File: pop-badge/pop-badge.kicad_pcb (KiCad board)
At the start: 2 copper layers, 129.5 x 101.3 mm, 158 parts, among them J1 Conn_01x04, Q1 BC818, U1 WS2812-2020, U10 WS2812-2020, U11 WS2812-2020, U12 WS2812-2020, U13 WS2812-2020, U14 WS2812-2020, U15 WS2812-2020, U16 WS2812-2020, U17 WS2812-2020, U18 WS2812-2020, U19 WS2812-2020, U2 WS2812-2020, U20 WS2812-2020, U21 WS2812-2020, U22 WS2812-2020, U23 WS2812-2020, U24 WS2812-2020, U25 WS2812-2020, U26 Pico, U3 WS2812-2020, U4 WS2812-2020, U5 WS2812-2020, U6 WS2812-2020, U7 WS2812-2020, U8 WS2812-2020, U9 WS2812-2020

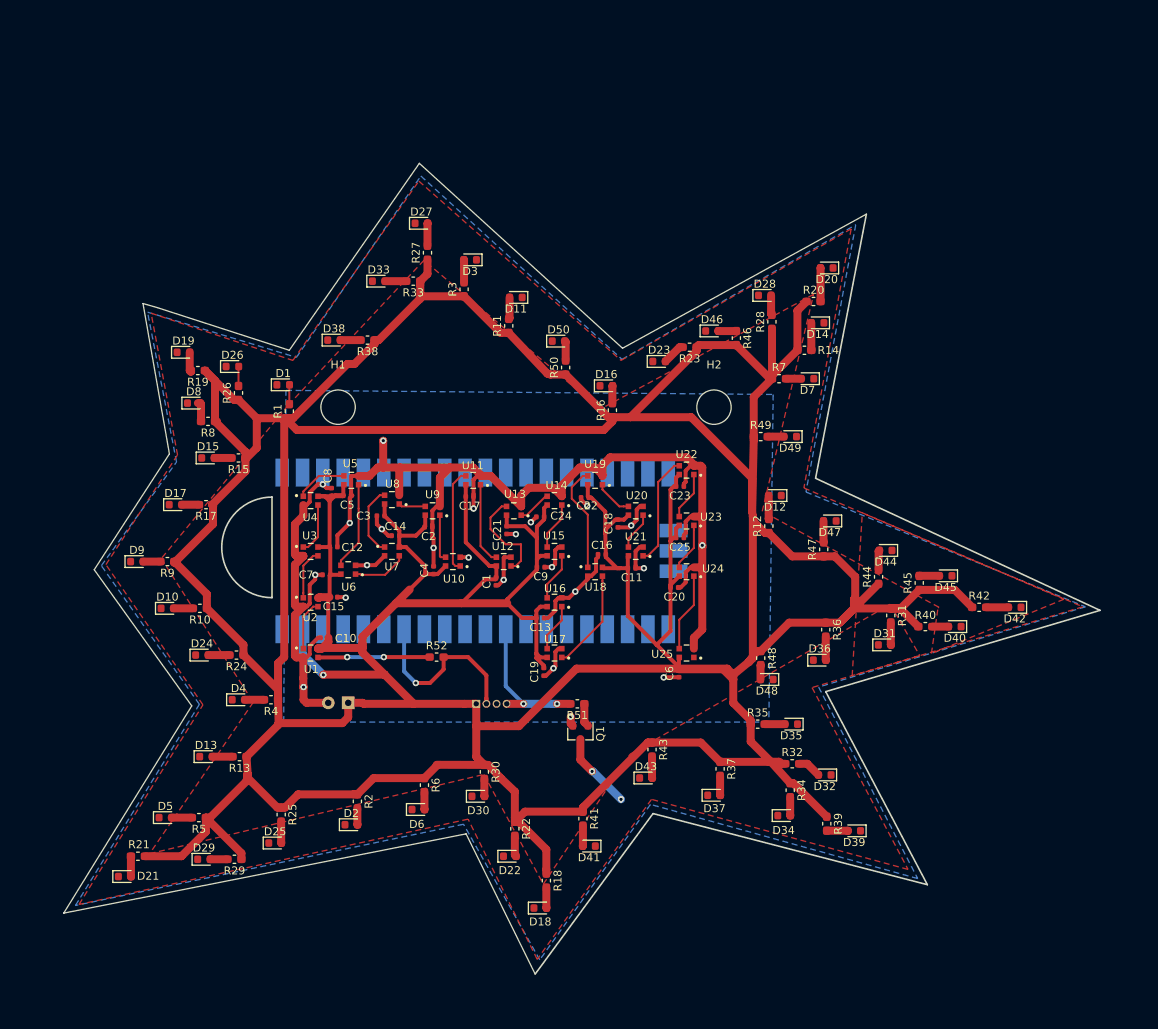
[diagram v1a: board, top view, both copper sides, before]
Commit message: redo power rails to avoid loops
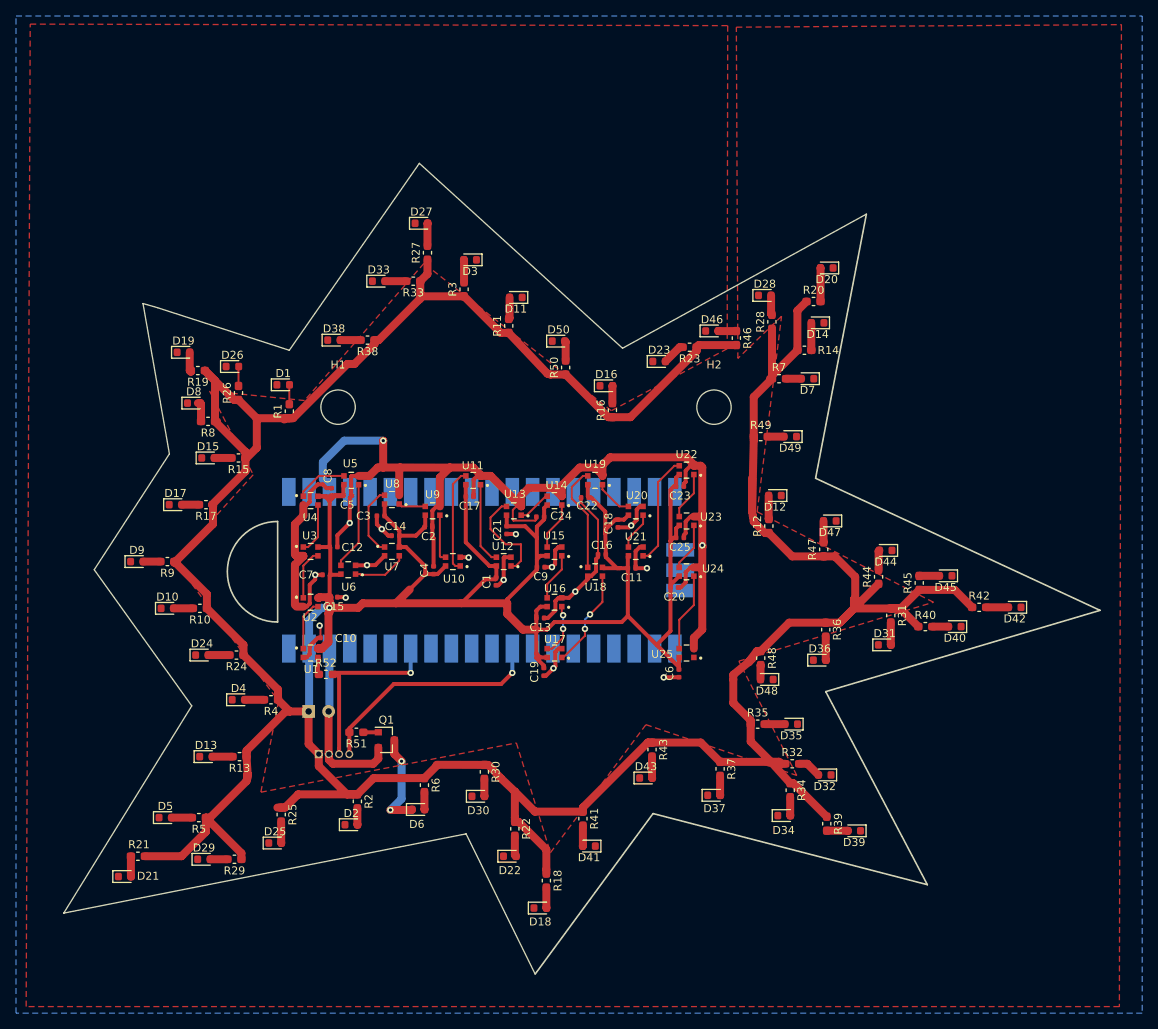
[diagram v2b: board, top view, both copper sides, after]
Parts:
- Q1: value BC818 -> S9013
- R1, R10, R11, R12, R13, R14, R15, R16, R17, R18, R19, R2, R20, R21, R22, R23, R24, R25, R26, R27, R28, R29, R3, R30, R31, R32, R33, R34, R35, R36, R37, R38, R39, R4, R40, R41, R42, R43, R44, R45, R46, R47, R48, R49, R5, R50, R6, R7, R8, R9: value 100 -> 200
- moved R51 27.9 mm to (50.5, 113.0)
- moved Q1 24.3 mm to (54.3, 114.0), turned to 0 degrees
- moved J1 20.7 mm to (45.8, 115.8)
- moved R52 14.0 mm to (46.7, 105.8)
- moved C26 5.07 mm to (44.6, 110.4), turned to 0 degrees
- moved U26 2.55 mm to (66.2, 92.8)
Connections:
- J1 pad 2: DIN -> GND
- J1 pad 3: GND -> DIN
- U26 pad 38: Net-(U26-Pad38) -> GND
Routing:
- net +5V: track 836.4 -> 651.1 mm
- net GND: track 222.9 -> 251.1 mm, vias 23 -> 17
- net Net-(R52-Pad1): track 14.1 -> 2.68 mm, vias 2 -> 0
- net LEDwMCU: track 19.1 -> 30.4 mm, vias 2 -> 1
- net LEDw-: track 9.72 -> 12.4 mm
- net Net-(Q1-Pad1): track 2.94 -> 1.87 mm
- net Net-(U16-Pad1): track 6.01 -> 6.67 mm, vias 0 -> 2
- net Net-(U17-Pad1): track 12.6 -> 12.5 mm, vias 0 -> 2
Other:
- outline, holes or cut-outs redrawn

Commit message: some silkscreen adjustments
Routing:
- net +5V: track 651.1 -> 647.8 mm
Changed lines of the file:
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@@
     (thickness 1.6)
     (drawings 19)
-    (tracks 726)
+    (tracks 727)
     (zones 0)
     (modules 158)
@@
     (39 F.Mask user)
     (40 Dwgs.User user)
-    (41 Cmts.User user hide)
+    (41 Cmts.User user)
     (42 Eco1.User user)
     (43 Eco2.User user)
@@
     (46 B.CrtYd user)
     (47 F.CrtYd user)
-    (48 B.Fab user hide)
-    (49 F.Fab user hide)
+    (48 B.Fab user)
+    (49 F.Fab user)
   )
   (setup
@@
     (tags "resistor handsolder")
     (attr smd)
-    (fp_text reference R51 (at 0 -1.43) (layer F.SilkS)
+    (fp_text reference R51 (at 0.0635 1.4605) (layer F.SilkS)
       (effects (font (size 1 1) (thickness 0.15)))
     )
@@
     (tags capacitor)
     (attr smd)
-    (fp_text reference C15 (at 0 -1.17) (layer F.SilkS)
+    (fp_text reference C15 (at -0.3175 -1.397) (layer F.SilkS)
       (effects (font (size 1 1) (thickness 0.15)))
     )
@@
     (descr "CP, Radial series, Radial, pin pitch=2.50mm, , diameter=6.3mm, Electrolytic Capacitor")
     (tags "CP Radial series Radial pin pitch 2.50mm  diameter 6.3mm Electrolytic Capacitor")
-    (fp_text reference C26 (at 1.27 -4.6355) (layer B.SilkS)
+    (fp_text reference C26 (at -4.1275 0.0635) (layer B.SilkS)
       (effects (font (size 1 1) (thickness 0.15)) (justify mirror))
     )
@@
     (tags "resistor handsolder")
     (attr smd)
-    (fp_text reference R52 (at 0 -1.43) (layer F.SilkS)
+    (fp_text reference R52 (at 0.254 1.7145) (layer F.SilkS)
       (effects (font (size 1 1) (thickness 0.15)))
     )
@@
   (module led:LED_WS2812-2020 (layer F.Cu)
     (at 68.961 91.694 180)
-    (fp_text reference U12 (at 0.127 1.905) (layer F.SilkS)
+    (fp_text reference U12 (at -1.0795 -1.905) (layer F.SilkS)
       (effects (font (size 1.00011 1.00011) (thickness 0.15)))
     )
@@
   (module led:LED_WS2812-2020 (layer F.Cu)
     (at 44.831 96.774)
-    (fp_text reference U2 (at -0.0635 1.905) (layer F.SilkS)
+    (fp_text reference U2 (at -0.0635 2.0955) (layer F.SilkS)
       (effects (font (size 1.00011 1.00011) (thickness 0.15)))
     )
@@
   (module led:LED_WS2812-2020 (layer F.Cu)
     (at 44.831 103.124)
-    (fp_text reference U1 (at 0.0635 2.032) (layer F.SilkS)
+    (fp_text reference U1 (at -3.048 0.1905) (layer F.SilkS)
       (effects (font (size 1.00011 1.00011) (thickness 0.15)))
     )
@@
     (tags "resistor handsolder")
     (attr smd)
-    (fp_text reference R39 (at 0 -1.43 90) (layer F.SilkS)
+    (fp_text reference R39 (at 0.0635 1.397 90) (layer F.SilkS)
       (effects (font (size 1 1) (thickness 0.15)))
     )
@@
     (tags diode)
     (attr smd)
-    (fp_text reference D25 (at 0 -1.43) (layer F.SilkS)
+    (fp_text reference D25 (at -0.0635 1.651) (layer F.SilkS)
       (effects (font (size 1 1) (thickness 0.15)))
     )
@@
     (tags diode)
     (attr smd)
-    (fp_text reference D8 (at 0 -1.43) (layer F.SilkS)
+    (fp_text reference D8 (at -2.6035 0) (layer F.SilkS)
       (effects (font (size 1 1) (thickness 0.15)))
     )
@@
     (tags diode)
     (attr smd)
-    (fp_text reference D2 (at 0 -1.43) (layer F.SilkS)
+    (fp_text reference D2 (at -0.0635 1.524) (layer F.SilkS)
       (effects (font (size 1 1) (thickness 0.15)))
     )
@@
   (segment (start 45.746 97.324) (end 45.146 97.324) (width 0.25) (layer F.Cu) (net 35) (status 10))
   (segment (start 38.1 73.773) (end 35.814 71.487) (width 1) (layer F.Cu) (net 80) (status 20))
-  (segment (start 42.164 73.773) (end 38.1 73.773) (width 1) (layer F.Cu) (net 80) (status 10))
   (segment (start 35.278 71.487) (end 35.814 71.487) (width 1) (layer F.Cu) (net 80) (status 20))
-  (segment (start 31.609 67.818) (end 35.278 71.487) (width 1) (layer F.Cu) (net 80) (status 10))
   (segment (start 32.879 74.168) (end 33.133 74.168) (width 1) (layer F.Cu) (net 80) (status 30))
   (segment (start 36.689 78.74) (end 36.689 78.881) (width 1) (layer F.Cu) (net 80) (status 30))
@@
   (segment (start 72.865 122.95) (end 78.867 122.95) (width 1) (layer F.Cu) (net 80))
   (segment (start 70.358 120.443) (end 72.865 122.95) (width 1) (layer F.Cu) (net 80))
+  (segment (start 42.164 74.298) (end 42.164 73.773) (width 1) (layer F.Cu) (net 80))
+  (segment (start 38.992 77.47) (end 42.164 74.298) (width 1) (layer F.Cu) (net 80))
+  (segment (start 38.1 77.47) (end 38.992 77.47) (width 1) (layer F.Cu) (net 80))
   (segment (start 49.671 115.7465) (end 49.657 115.7605) (width 0.5) (layer F.Cu) (net 81) (status 30))
   (segment (start 49.671 113.03) (end 49.671 115.7465) (width 0.5) (layer F.Cu) (net 81) (status 30))

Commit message: use proper pin connector and expose LEDw- on connector
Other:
- board text added: "+5V"
- board text added: "DIN (WS2812b)"
- board text added: "GND"
- board text added: "PWM (white LEDs)"
- board text added: "Twäng Pop! Badge V0.5 Docs: https://github.com/jrudolph/twaeng-pop-badge"
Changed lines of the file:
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@@
   (general
     (thickness 1.6)
-    (drawings 19)
+    (drawings 24)
     (tracks 727)
     (zones 0)
@@
     )
   )
+  (gr_text "PWM (white LEDs)" (at 46.4439 121.2215 45) (layer B.SilkS)
+    (effects (font (size 0.8 0.8) (thickness 0.16)) (justify mirror))
+  )
+  (gr_text "DIN (WS2812b)" (at 45.4787 120.628878 45) (layer B.SilkS)
+    (effects (font (size 0.8 0.8) (thickness 0.16)) (justify mirror))
+  )
+  (gr_text GND (at 46.4693 118.258386 45) (layer B.SilkS)
+    (effects (font (size 0.8 0.8) (thickness 0.16)) (justify mirror))
+  )
+  (gr_text +5V (at 45.1231 118.258386 45) (layer B.SilkS)
+    (effects (font (size 0.8 0.8) (thickness 0.16)) (justify mirror))
+  )
+  (gr_text "Twäng Pop! Badge V0.5\nDocs: https://github.com/jrudolph/twaeng-pop-badge" (at 85.4075 117.4115) (layer B.SilkS)
+    (effects (font (size 1 1) (thickness 0.15)) (justify mirror))
+  )
   (gr_arc (start 40.7035 92.964) (end 40.7035 86.6775) (angle -180) (layer Edge.Cuts) (width 0.2))

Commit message: add twaeng sign
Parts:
- J1: value Conn_01x04 -> Conn_01x05; footprint Connector_PinHeader_1.27mm:PinHeader_1x04_P1.27mm_Vertical -> Connector_PinSocket_2.54mm:PinSocket_1x05_P2.54mm_Vertical
- moved Q1 2.78 mm to (56.8, 112.9)
- moved R51 2.78 mm to (53.1, 111.9)
- moved J1 1.63 mm to (44.6, 116.8)
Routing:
- net GND: track 251.1 -> 245.6 mm, vias 17 -> 18
- net LEDw-: track 12.4 -> 15.1 mm, vias 2 -> 1
- net +5V: track 647.8 -> 645.3 mm
- net DIN: track 24.3 -> 25.9 mm
- net LEDwMCU: track 30.4 -> 29.6 mm
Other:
- board text added: "LED-"

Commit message: add alternative path
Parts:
- added G***: LOGO, twaeng:sign, F.Cu at (63.2, 71.5)
- added JP1: SolderJumper_2_Open, Jumper:SolderJumper-2_P1.3mm_Open_Pad1.0x1.5mm, F.Cu at (55.5, 109.3)
- added JP2: FET Closed, Jumper:SolderJumper-2_P1.3mm_Bridged_Pad1.0x1.5mm, F.Cu at (55.5, 113.3)
- added Q2: AO3400A, footprints:SOT95P280X125-3N, F.Cu at (61.5, 114.4)
- added R53: 200, Resistor_SMD:R_0603_1608Metric_Pad1.05x0.95mm_HandSolder, F.Cu at (58.2, 112.5)
- R51: value 4k7 -> 82
- R52: value 220R -> 200
- moved R51 5.87 mm to (58.2, 109.0), turned to 270 degrees
- moved Q1 5.59 mm to (61.0, 109.1)
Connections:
- R51 pad 2: LEDwMCU -> Net-(JP1-Pad2)
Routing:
- net LEDw-: track 15.1 -> 27.4 mm, vias 1 -> 2
- net Net-(Q2-Pad1): track 0.00 -> 2.81 mm
- net Net-(JP1-Pad2): track 0.00 -> 2.22 mm
- net Net-(JP2-Pad2): track 0.00 -> 2.06 mm
- net GND: track 245.6 -> 247.2 mm, vias 18 -> 19
- net LEDwMCU: track 29.6 -> 30.6 mm

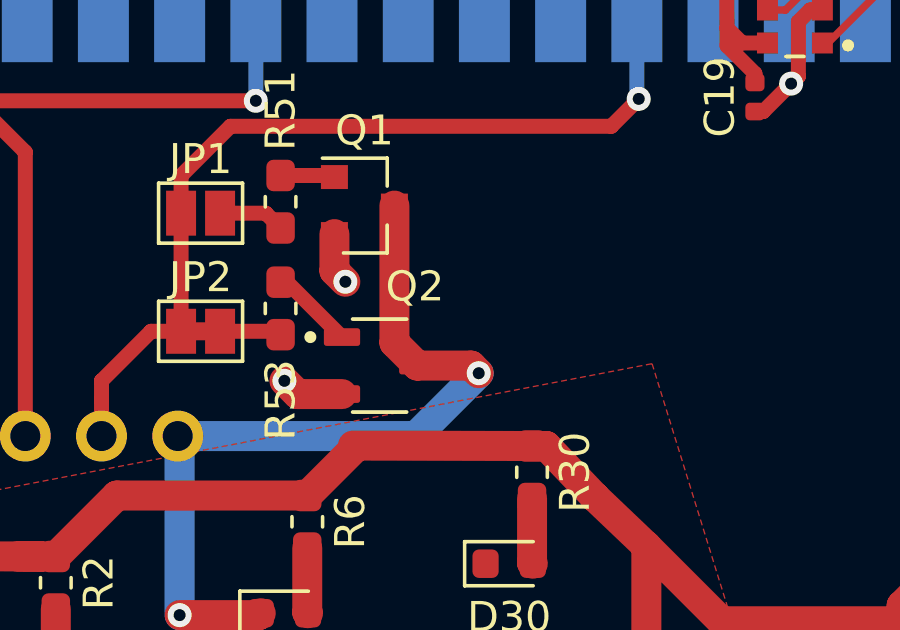
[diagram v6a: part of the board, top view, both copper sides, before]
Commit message: add pull down for mosfet
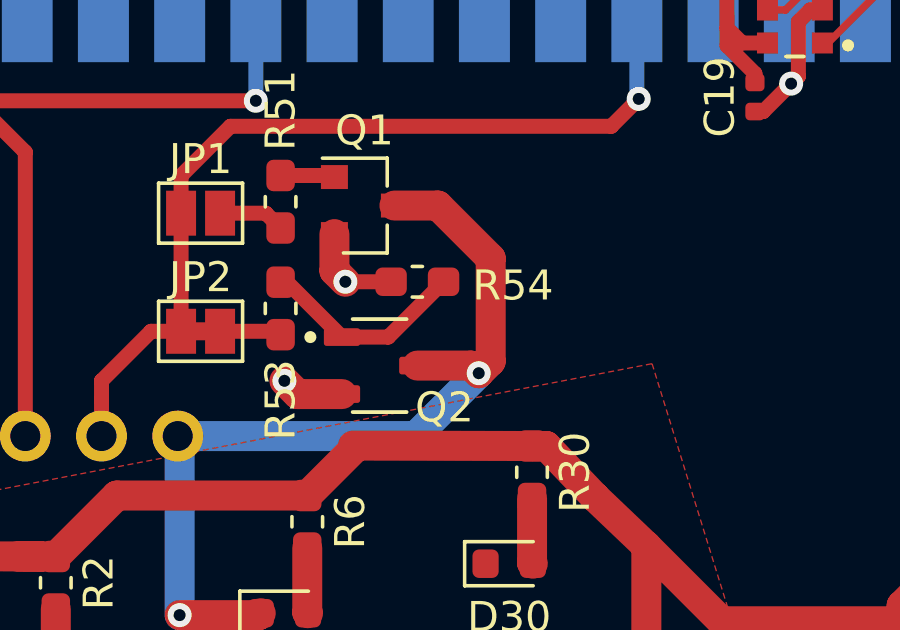
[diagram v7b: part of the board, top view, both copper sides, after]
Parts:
- added R54: 100k, Resistor_SMD:R_0603_1608Metric_Pad1.05x0.95mm_HandSolder, F.Cu at (62.7, 111.6)
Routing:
- net Net-(Q2-Pad1): track 2.81 -> 6.95 mm
- net LEDw-: track 27.4 -> 29.7 mm
- net GND: track 247.2 -> 248.7 mm
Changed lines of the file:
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@@
     (thickness 1.6)
     (drawings 25)
-    (tracks 740)
+    (tracks 745)
     (zones 0)
-    (modules 163)
+    (modules 164)
     (nets 124)
   )
   (page A4)
   (layers
-    (0 F.Cu signal)
+    (0 F.Cu signal hide)
     (31 B.Cu signal hide)
     (32 B.Adhes user hide)
@@
     (add_net "Net-(U8-Pad1)")
   )
+  (module Resistor_SMD:R_0603_1608Metric_Pad1.05x0.95mm_HandSolder (layer F.Cu)
+    (at 62.724 111.633)
+    (descr "Resistor SMD 0603 (1608 Metric), square (rectangular) end terminal, IPC_7351 nominal with elongated pad for handsoldering. (Body size source: http://www.tortai-tech.com/upload/download/2011102023233369053.pdf), generated with kicad-footprint-generator")
+    (tags "resistor handsolder")
+    (attr smd)
+    (fp_text reference R54 (at 3.189 0.127) (layer F.SilkS)
+      (effects (font (size 1 1) (thickness 0.15)))
+    )
+    (fp_text value 100k (at 0 1.43) (layer F.Fab)
+      (effects (font (size 1 1) (thickness 0.15)))
+    )
+    (fp_text user %R (at 0 0) (layer F.Fab)
+      (effects (font (size 0.4 0.4) (thickness 0.06)))
+    )
+    (fp_line (start 1.65 0.73) (end -1.65 0.73) (layer F.CrtYd) (width 0.05))
+    (fp_line (start 1.65 -0.73) (end 1.65 0.73) (layer F.CrtYd) (width 0.05))
+    (fp_line (start -1.65 -0.73) (end 1.65 -0.73) (layer F.CrtYd) (width 0.05))
+    (fp_line (start -1.65 0.73) (end -1.65 -0.73) (layer F.CrtYd) (width 0.05))
+    (fp_line (start -0.171267 0.51) (end 0.171267 0.51) (layer F.SilkS) (width 0.12))
+    (fp_line (start -0.171267 -0.51) (end 0.171267 -0.51) (layer F.SilkS) (width 0.12))
+    (fp_line (start 0.8 0.4) (end -0.8 0.4) (layer F.Fab) (width 0.1))
+    (fp_line (start 0.8 -0.4) (end 0.8 0.4) (layer F.Fab) (width 0.1))
+    (fp_line (start -0.8 -0.4) (end 0.8 -0.4) (layer F.Fab) (width 0.1))
+    (fp_line (start -0.8 0.4) (end -0.8 -0.4) (layer F.Fab) (width 0.1))
+    (pad 2 smd roundrect (at 0.875 0) (size 1.05 0.95) (layers F.Cu F.Paste F.Mask) (roundrect_rratio 0.25)
+      (net 123 "Net-(Q2-Pad1)"))
+    (pad 1 smd roundrect (at -0.875 0) (size 1.05 0.95) (layers F.Cu F.Paste F.Mask) (roundrect_rratio 0.25)
+      (net 32 GND))
+    (model ${KISYS3DMOD}/Resistor_SMD.3dshapes/R_0603_1608Metric.wrl
+      (at (xyz 0 0 0))
+      (scale (xyz 1 1 1))
+      (rotate (xyz 0 0 0))
+    )
+  )
   (module Jumper:SolderJumper-2_P1.3mm_Open_Pad1.0x1.5mm (layer F.Cu)
     (at 55.499 109.347)
@@
   (module footprints:SOT95P280X125-3N (layer F.Cu)
     (at 61.468 114.427)
-    (fp_text reference Q2 (at 1.175 -2.635) (layer F.SilkS)
+    (fp_text reference Q2 (at 2.159 1.397) (layer F.SilkS)
       (effects (font (size 1 1) (thickness 0.15)))
     )
@@
   (segment (start 54.8005 117.1575) (end 54.8005 122.7455) (width 1) (layer B.Cu) (net 2) (status 10))
   (segment (start 54.737 117.094) (end 54.8005 117.1575) (width 1) (layer B.Cu) (net 2) (status 30))
-  (segment (start 61.96 113.664) (end 62.723 114.427) (width 1) (layer F.Cu) (net 2))
-  (segment (start 61.96 109.093) (end 61.96 113.664) (width 1) (layer F.Cu) (net 2))
   (via (at 64.77 114.681) (size 0.8) (drill 0.4) (layers F.Cu B.Cu) (net 2))
   (segment (start 64.516 114.427) (end 64.77 114.681) (width 1) (layer F.Cu) (net 2))
@@
   (segment (start 62.6745 116.7765) (end 54.737 116.7765) (width 1) (layer B.Cu) (net 2))
   (segment (start 64.77 114.681) (end 62.6745 116.7765) (width 1) (layer B.Cu) (net 2))
+  (segment (start 65.169999 114.281001) (end 64.77 114.681) (width 1) (layer F.Cu) (net 2))
+  (segment (start 65.169999 110.852999) (end 65.169999 114.281001) (width 1) (layer F.Cu) (net 2))
+  (segment (start 63.41 109.093) (end 65.169999 110.852999) (width 1) (layer F.Cu) (net 2))
+  (segment (start 61.96 109.093) (end 63.41 109.093) (width 1) (layer F.Cu) (net 2))
   (segment (start 50.673 124.5615) (end 50.6985 124.587) (width 1) (layer F.Cu) (net 3) (status 30))
   (segment (start 50.673 122.541) (end 50.673 124.5615) (width 1) (layer F.Cu) (net 3) (status 30))
@@
   (segment (start 58.735 115.377) (end 58.293 114.935) (width 1) (layer F.Cu) (net 32))
   (segment (start 60.213 115.377) (end 58.735 115.377) (width 1) (layer F.Cu) (net 32))
+  (segment (start 61.849 111.633) (end 60.325 111.633) (width 0.5) (layer F.Cu) (net 32))
   (via (at 57.3405 105.6005) (size 0.8) (drill 0.4) (layers F.Cu B.Cu) (net 33))
   (segment (start 57.3405 101.6635) (end 57.3405 105.6005) (width 0.5) (layer B.Cu) (net 33) (status 10))
@@
   (segment (start 58.383 111.647) (end 60.213 113.477) (width 0.5) (layer F.Cu) (net 123))
   (segment (start 58.166 111.647) (end 58.383 111.647) (width 0.5) (layer F.Cu) (net 123))
+  (segment (start 61.755 113.477) (end 60.213 113.477) (width 0.5) (layer F.Cu) (net 123))
+  (segment (start 63.599 111.633) (end 61.755 113.477) (width 0.5) (layer F.Cu) (net 123))
   (zone (net 2) (net_name LEDw-) (layer F.Cu) (hatch edge 0.508)
     (connect_pads (clearance 0.508))
